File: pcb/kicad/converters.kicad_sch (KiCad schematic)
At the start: 49 parts, among them U6 PCM5122PW, U7 74LVC1G32, U8 PCM1863DBT, Y1 22.5792MHz, Y2 24.576MHz

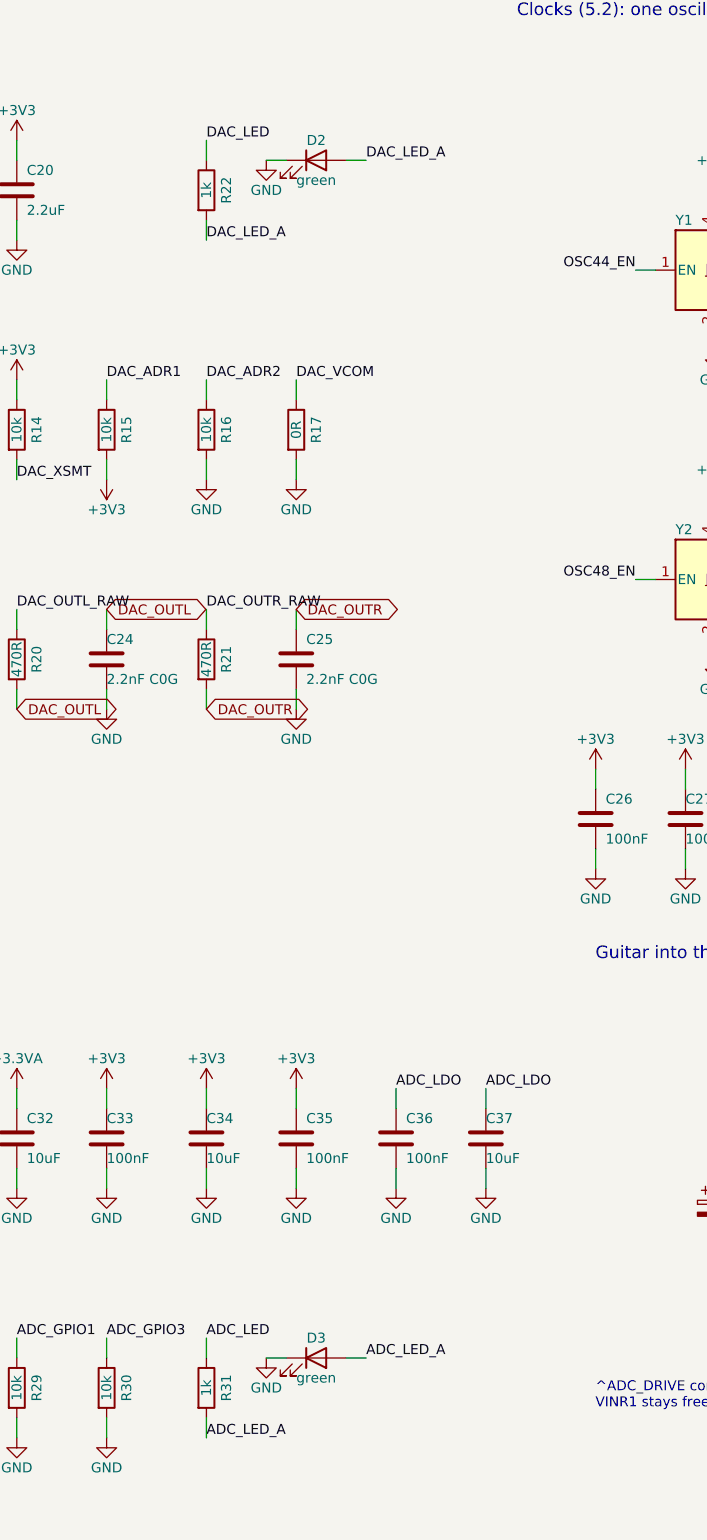
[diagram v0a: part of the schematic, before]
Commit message: Pedalboard PCB: guitar input and outputs sheets
Guitar input: 5 V reference, protected 1 Mohm input, OPA1642 gain
stage (0 to +24 dB), LM393 clip LED with a hold. Outputs: main volume,
OPA1642 buffers and impedance-balanced TRS jacks; headphone volume into
the TPA6130A2, with 10k ahead of the knob to keep its inputs in range.

Co-Authored-By: Claude Opus 5.5 <noreply@anthropic.com>
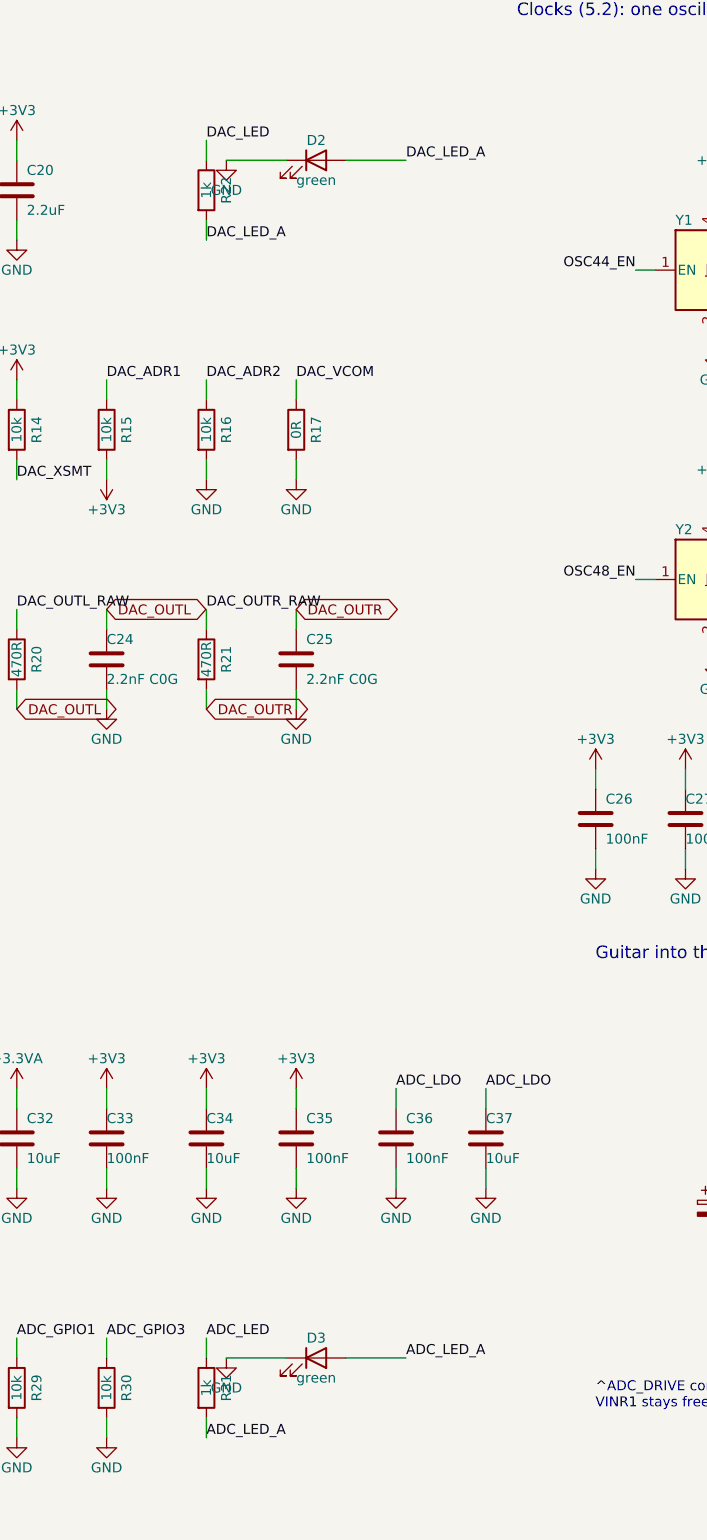
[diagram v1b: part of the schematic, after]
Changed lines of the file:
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@@
 		(pts
 			(xy 200.66 66.04)
-			(xy 198.12 66.04)
+			(xy 193.04 66.04)
 		)
 		(stroke
@@
 	(symbol
 		(lib_id "power:GND")
-		(at 198.12 66.04 0)
+		(at 193.04 66.04 0)
 		(unit 1)
 		(exclude_from_sim no)
@@
 		(dnp no)
 		(property "Reference" "#PWR023"
-			(at 198.12 72.39 0)
+			(at 193.04 72.39 0)
 			(effects
 				(font
@@
 		)
 		(property "Value" "GND"
-			(at 198.12 69.85 0)
+			(at 193.04 69.85 0)
 			(effects
 				(font
@@
 		)
 		(property "Footprint" ""
-			(at 198.12 66.04 0)
+			(at 193.04 66.04 0)
 			(effects
 				(font
@@
 		)
 		(property "Datasheet" ""
-			(at 198.12 66.04 0)
+			(at 193.04 66.04 0)
 			(effects
 				(font
@@
 		)
 		(property "Description" "Power symbol creates a global label with name \"GND\" , ground"
-			(at 198.12 66.04 0)
+			(at 193.04 66.04 0)
 			(effects
 				(font
@@
 		(pts
 			(xy 208.28 66.04)
-			(xy 210.82 66.04)
+			(xy 215.9 66.04)
 		)
 		(stroke
@@
 	)
 	(label "DAC_LED_A"
-		(at 210.82 66.04 0)
+		(at 215.9 66.04 0)
 		(effects
 			(font
@@
 		(pts
 			(xy 200.66 218.44)
-			(xy 198.12 218.44)
+			(xy 193.04 218.44)
 		)
 		(stroke
@@
 	(symbol
 		(lib_id "power:GND")
-		(at 198.12 218.44 0)
+		(at 193.04 218.44 0)
 		(unit 1)
 		(exclude_from_sim no)
@@
 		(dnp no)
 		(property "Reference" "#PWR061"
-			(at 198.12 224.79 0)
+			(at 193.04 224.79 0)
 			(effects
 				(font
@@
 		)
 		(property "Value" "GND"
-			(at 198.12 222.25 0)
+			(at 193.04 222.25 0)
 			(effects
 				(font
@@
 		)
 		(property "Footprint" ""
-			(at 198.12 218.44 0)
+			(at 193.04 218.44 0)
 			(effects
 				(font
@@
 		)
 		(property "Datasheet" ""
-			(at 198.12 218.44 0)
+			(at 193.04 218.44 0)
 			(effects
 				(font
@@
 		)
 		(property "Description" "Power symbol creates a global label with name \"GND\" , ground"
-			(at 198.12 218.44 0)
+			(at 193.04 218.44 0)
 			(effects
 				(font
@@
 		(pts
 			(xy 208.28 218.44)
-			(xy 210.82 218.44)
+			(xy 215.9 218.44)
 		)
 		(stroke
@@
 	)
 	(label "ADC_LED_A"
-		(at 210.82 218.44 0)
+		(at 215.9 218.44 0)
 		(effects
 			(font

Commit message: Pedalboard PCB: first layout, and Alps RK09L pots
A 4-layer, 208 x 90 mm board, placed and routed from the netlist: the
jacks, knobs, button and clip LED meet the rear panel at the board edge
(from the makers' drawings), small parts sit at the pins the schematic
names, ground plane on In1, routed with Freerouting. Not finished:
4 nets left unrouted, silkscreen to tidy, 3D check to do.

All three knobs are now Alps RK09L12B0A4S (dual 10k log, M9 thread):
the RK09K had no threaded bushing and Alps makes no 50k log single-gang
RK09L. The gain stage's resistors are scaled by 1/5 to keep the same
gain (simulations A1-A3, A5, A7 re-run: pass, noise 1.0 dB). Footprints
from the symbol libraries are kept (14 parts had none), and the MIDI
jack has its own footprint (pedalboard.pretty).

Co-Authored-By: Claude Opus 5.5 <noreply@anthropic.com>
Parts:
- U6: footprint (none) -> Package_SO:TSSOP-28_4.4x9.7mm_P0.65mm
- U8: footprint (none) -> Package_SO:TSSOP-30_4.4x7.8mm_P0.5mm
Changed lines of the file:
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@@
 			)
 		)
-		(property "Footprint" ""
+		(property "Footprint" "Package_SO:TSSOP-28_4.4x9.7mm_P0.65mm"
 			(at 74.93 105.41 0)
 			(effects
@@
 			)
 		)
-		(property "Footprint" ""
+		(property "Footprint" "Package_SO:TSSOP-30_4.4x7.8mm_P0.5mm"
 			(at 74.93 219.71 0)
 			(effects

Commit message: Pedalboard PCB: maker part numbers and LCSC numbers on every part
Each part on the schematic and the board now carries Manufacturer, MPN
and LCSC fields, for the PCBWay and JLCPCB assembly BOMs. FB1 is the
2 A bead (no 0805 bead is rated 3 A), F1 the MF-MSMF150-2 fuse. The
drill/place origin is the board's bottom-left corner, so the Gerbers,
drill and placement files measure from the board.

Co-Authored-By: Claude Opus 5.5 <noreply@anthropic.com>
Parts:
- C17, C18, C23, C26, C27, C28, C30, C31, C33, C35, C36: LCSC (none) -> C14663; MPN (none) -> CC0603KRX7R9BB104; Manufacturer (none) -> YAGEO
- C19, C32, C34, C37: LCSC (none) -> C15850; MPN (none) -> CL21A106KAYNNNE; Manufacturer (none) -> Samsung
- C20, C21, C22: LCSC (none) -> C23630; MPN (none) -> CL10A225KO8NNNC; Manufacturer (none) -> Samsung
- C24, C25: LCSC (none) -> C107043; MPN (none) -> CC0603JRNPO9BN222; Manufacturer (none) -> YAGEO
- C29: LCSC (none) -> C15849; MPN (none) -> CL10A105KB8NNNC; Manufacturer (none) -> Samsung
- C38: LCSC (none) -> C72486; MPN (none) -> RVT1V100M0505; Manufacturer (none) -> ROQANG
- C39: LCSC (none) -> C441760; MPN (none) -> GRM2195C1H103FA01D; Manufacturer (none) -> Murata
- D2, D3: LCSC (none) -> C99289; MPN (none) -> LTST-C191GKT; Manufacturer (none) -> Lite-On
- R14, R15, R16, R28, R29, R30: LCSC (none) -> C25804; MPN (none) -> 0603WAF1002T5E; Manufacturer (none) -> UNI-ROYAL
- R17, R26: LCSC (none) -> C21189; MPN (none) -> 0603WAF0000T5E; Manufacturer (none) -> UNI-ROYAL
- R18, R19, R25, R27: LCSC (none) -> C23140; MPN (none) -> 0603WAF330JT5E; Manufacturer (none) -> UNI-ROYAL
- R20, R21: LCSC (none) -> C23179; MPN (none) -> 0603WAF4700T5E; Manufacturer (none) -> UNI-ROYAL
- R22, R31: LCSC (none) -> C21190; MPN (none) -> 0603WAF1001T5E; Manufacturer (none) -> UNI-ROYAL
- R23, R24: LCSC (none) -> C25819; MPN (none) -> 0603WAF4702T5E; Manufacturer (none) -> UNI-ROYAL
- R32: LCSC (none) -> C22775; MPN (none) -> 0603WAF1000T5E; Manufacturer (none) -> UNI-ROYAL
- U6: LCSC (none) -> C962071; MPN (none) -> PCM5122PWR; Manufacturer (none) -> Texas Instruments
- U7: LCSC (none) -> C10096; MPN (none) -> SN74LVC1G32DBVR; Manufacturer (none) -> Texas Instruments
- U8: LCSC (none) -> C529569; MPN (none) -> PCM1863DBTR; Manufacturer (none) -> Texas Instruments
- Y1, Y2: Manufacturer (none) -> Kyocera
